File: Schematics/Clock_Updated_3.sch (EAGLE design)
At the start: 48 parts, among them U1 ATMEGA328P

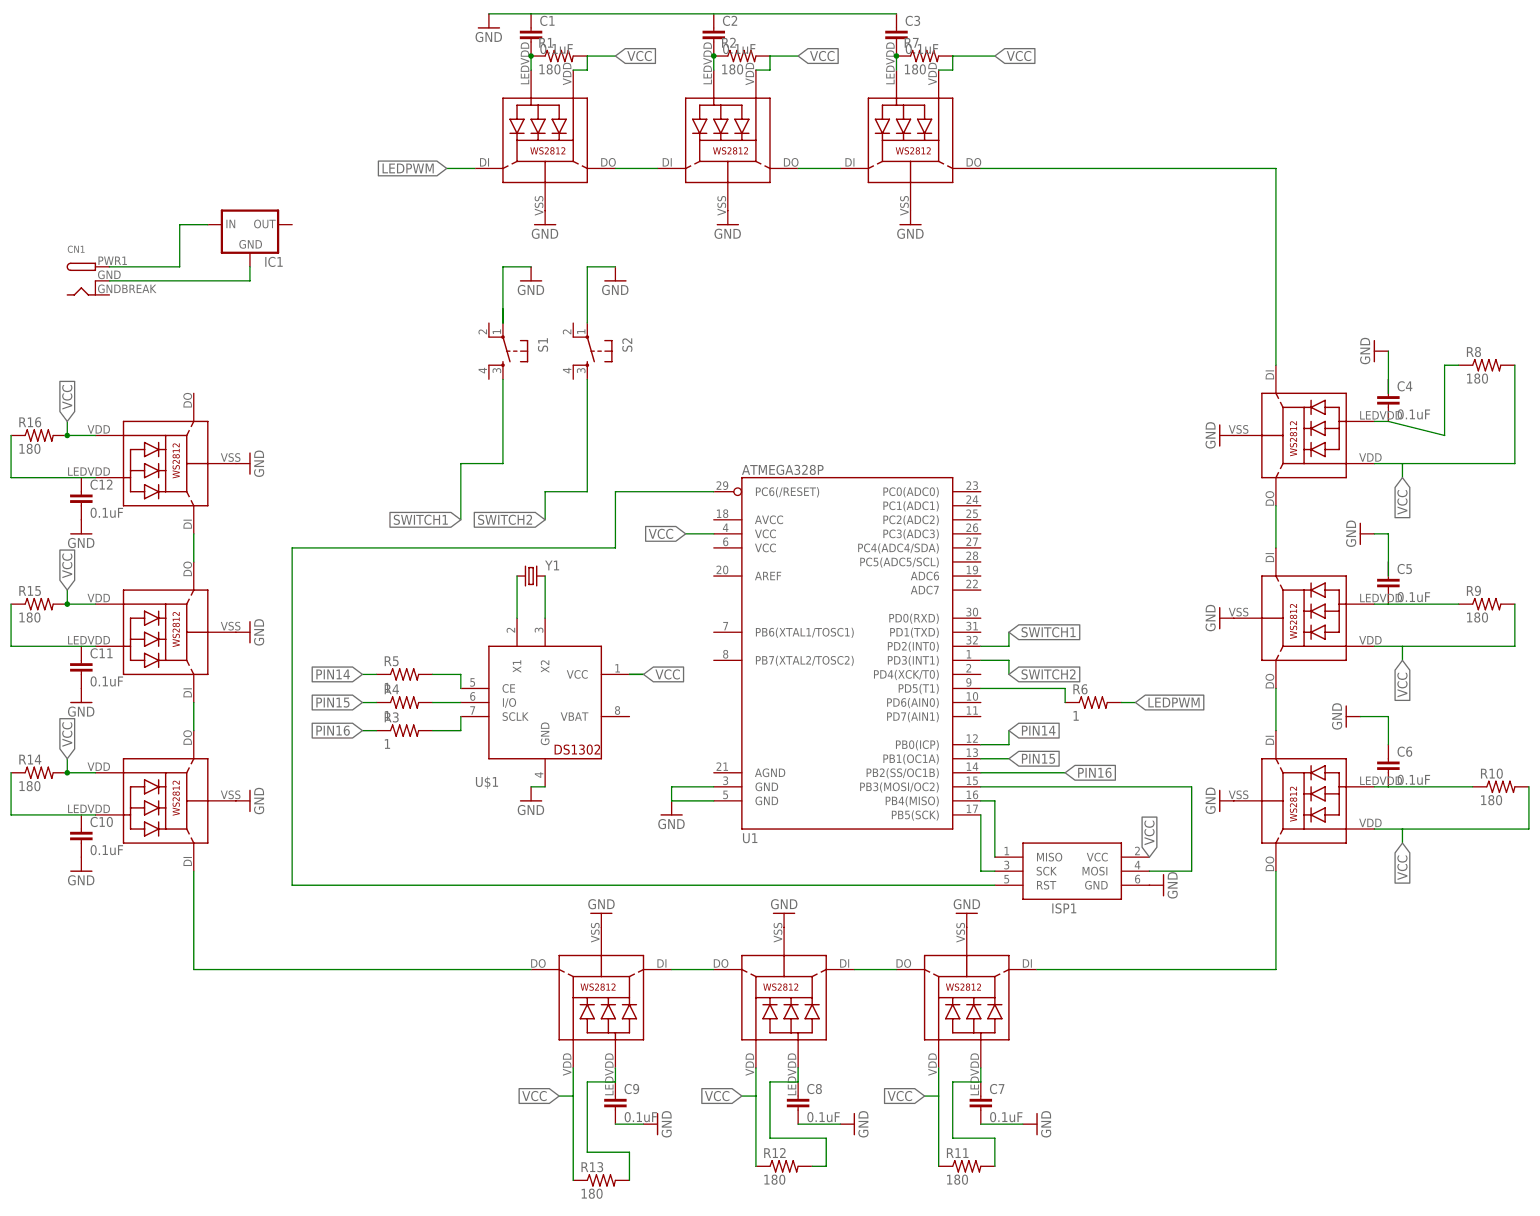
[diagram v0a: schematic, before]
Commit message: line color change
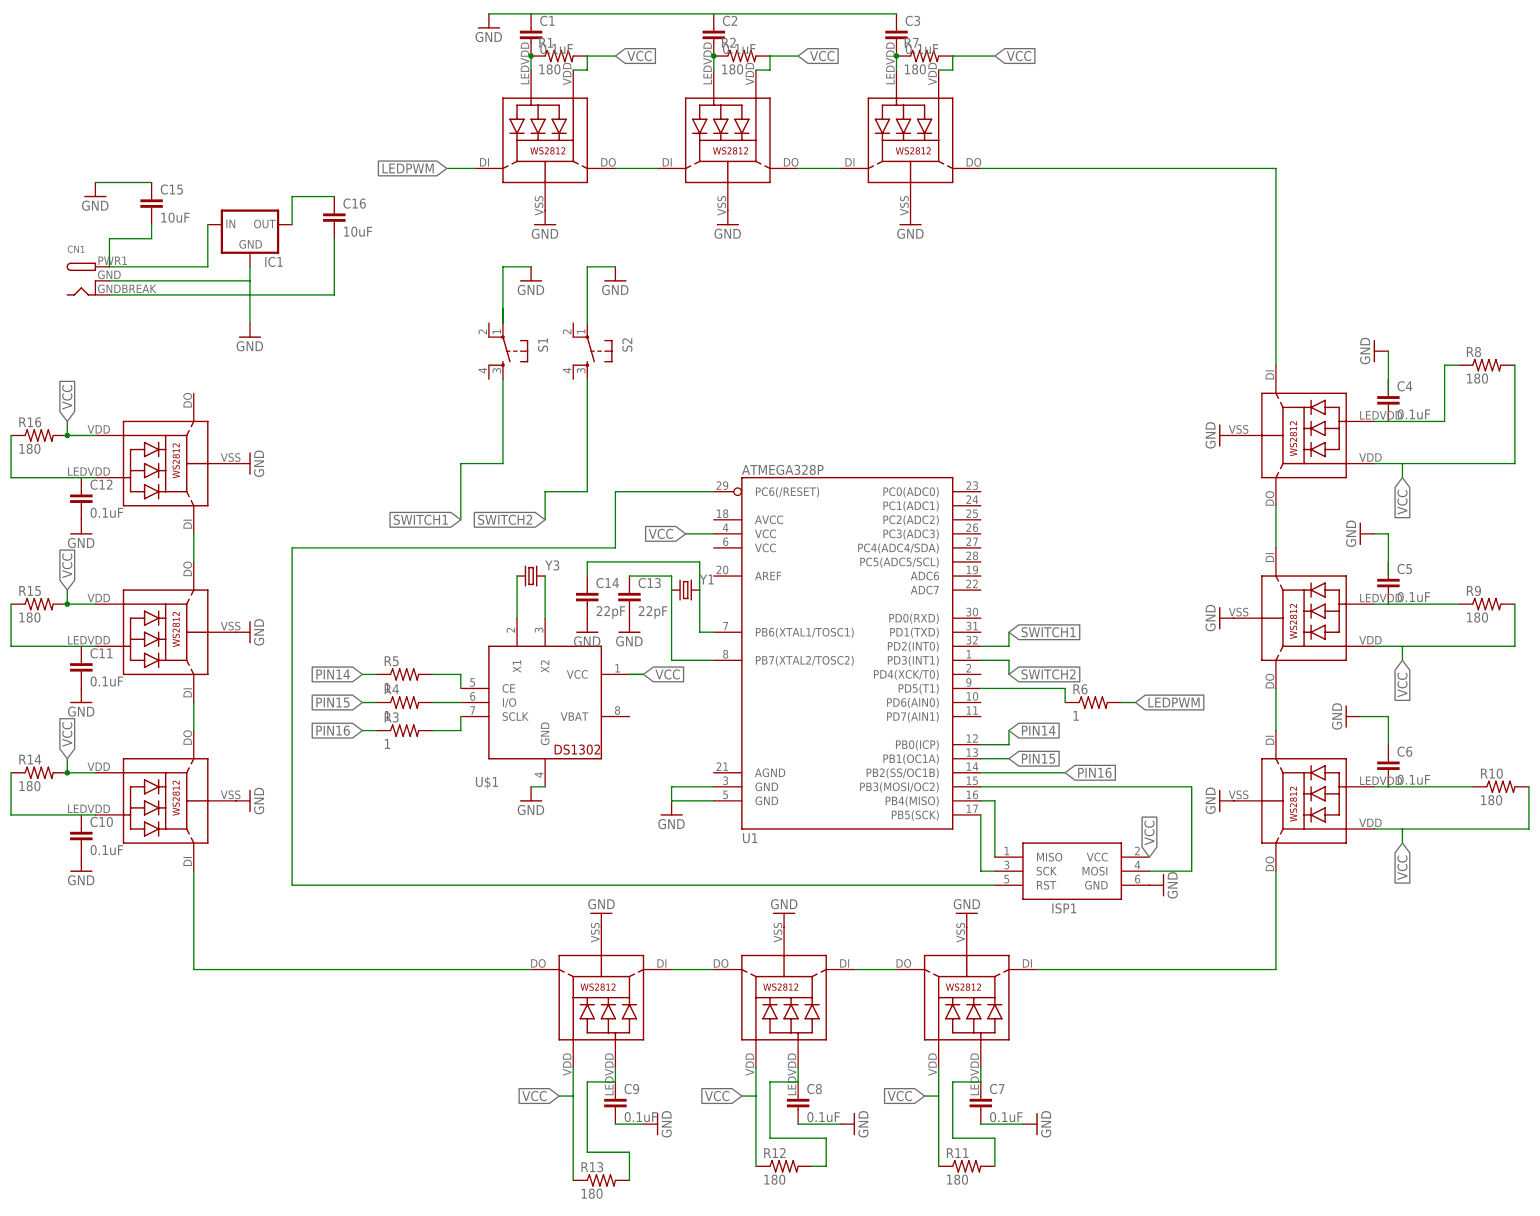
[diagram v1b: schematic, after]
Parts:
- added C13, C14: 22pF, SparkFun-Capacitors:22PF-50V-5%(0603)
- added C15, C16: 10uF, SparkFun-Capacitors:10UF-6.3V-20%(1206)
- added Y3: (no value), SparkFun-FreqCtrl:CRYSTAL32-SMD
- Y1: device SparkFun-FreqCtrl:CRYSTALTC38H -> SparkFun-FreqCtrl:CRYSTALSMD
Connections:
- new net N$38: C13.1, U1.PB7(XTAL2/TOSC2), Y1.1
- new net N$39: C14.1, U1.PB6(XTAL1/TOSC1), Y1.2
- net GND: now also C13.2, C14.2, C15.1, C16.2, CN1.GND, CN1.GNDBREAK, IC1.GND
- net N$36: now also C15.2
- net N$37: now also C16.1, IC1.OUT; no longer CN1.GNDBREAK, IC1.GND
- net N$7: now also Y3.2; no longer Y1.2
- net N$8: now also Y3.1; no longer Y1.1
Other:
- moved on the sheet: Y1
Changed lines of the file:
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@@
 </classes>
 <parts>
-<part name="Y1" library="SparkFun-FreqCtrl" deviceset="CRYSTAL" device="TC38H"/>
 <part name="S1" library="SparkFun-Electromechanical" deviceset="TAC_SWITCH" device="PTH"/>
 <part name="S2" library="SparkFun-Electromechanical" deviceset="TAC_SWITCH" device="PTH"/>
@@
 <part name="GND26" library="supply1" deviceset="GND" device=""/>
 <part name="GND27" library="supply1" deviceset="GND" device=""/>
+<part name="C13" library="SparkFun-Capacitors" deviceset="22PF-50V-5%(0603)" device="" value="22pF"/>
+<part name="C14" library="SparkFun-Capacitors" deviceset="22PF-50V-5%(0603)" device="" value="22pF"/>
+<part name="GND28" library="supply1" deviceset="GND" device=""/>
+<part name="GND29" library="supply1" deviceset="GND" device=""/>
+<part name="Y3" library="SparkFun-FreqCtrl" deviceset="CRYSTAL" device="32-SMD"/>
+<part name="Y1" library="SparkFun-FreqCtrl" deviceset="CRYSTAL" device="SMD"/>
+<part name="GND30" library="supply1" deviceset="GND" device=""/>
+<part name="C15" library="SparkFun-Capacitors" deviceset="10UF-6.3V-20%(1206)" device="" value="10uF"/>
+<part name="C16" library="SparkFun-Capacitors" deviceset="10UF-6.3V-20%(1206)" device="" value="10uF"/>
+<part name="GND31" library="supply1" deviceset="GND" device=""/>
 </parts>
 <sheets>
@@
 </plain>
 <instances>
-<instance part="Y1" gate="G$1" x="30.48" y="53.34"/>
 <instance part="S1" gate="S" x="25.4" y="93.98" rot="R270"/>
 <instance part="S2" gate="S" x="40.64" y="93.98" rot="R270"/>
@@
 <instance part="GND26" gate="1" x="-50.8" y="0"/>
 <instance part="GND27" gate="1" x="144.78" y="-2.54" rot="R90"/>
+<instance part="C13" gate="G$1" x="48.26" y="48.26"/>
+<instance part="C14" gate="G$1" x="40.64" y="48.26"/>
+<instance part="GND28" gate="1" x="48.26" y="43.18"/>
+<instance part="GND29" gate="1" x="40.64" y="43.18"/>
+<instance part="Y3" gate="G$1" x="30.48" y="53.34"/>
+<instance part="Y1" gate="G$1" x="58.42" y="50.8"/>
+<instance part="GND30" gate="1" x="-20.32" y="96.52"/>
+<instance part="C15" gate="G$1" x="-38.1" y="119.38"/>
+<instance part="C16" gate="G$1" x="-5.08" y="116.84"/>
+<instance part="GND31" gate="1" x="-48.26" y="121.92"/>
 </instances>
 <busses>
@@
 <segment>
 <pinref part="U$1" gate="G$1" pin="X2"/>
-<pinref part="Y1" gate="G$1" pin="2"/>
 <wire x1="33.02" y1="53.34" x2="33.02" y2="45.72" width="0.1524" layer="91"/>
+<pinref part="Y3" gate="G$1" pin="2"/>
 </segment>
 </net>
@@
 <segment>
 <pinref part="U$1" gate="G$1" pin="X1"/>
-<pinref part="Y1" gate="G$1" pin="1"/>
 <wire x1="27.94" y1="53.34" x2="27.94" y2="45.72" width="0.1524" layer="91"/>
+<pinref part="Y3" gate="G$1" pin="1"/>
 </segment>
 </net>
@@
 <pinref part="ISP1" gate="G$1" pin="GND"/>
 <pinref part="GND27" gate="1" pin="GND"/>
+</segment>
+<segment>
+<pinref part="C13" gate="G$1" pin="2"/>
+<pinref part="GND28" gate="1" pin="GND"/>
+</segment>
+<segment>
+<pinref part="C14" gate="G$1" pin="2"/>
+<pinref part="GND29" gate="1" pin="GND"/>
+</segment>
+<segment>
+<pinref part="CN1" gate="G$1" pin="GNDBREAK"/>
+<pinref part="IC1" gate="G$1" pin="GND"/>
+<wire x1="-45.72" y1="106.68" x2="-20.32" y2="106.68" width="0.1524" layer="91"/>
+<wire x1="-20.32" y1="106.68" x2="-20.32" y2="109.22" width="0.1524" layer="91"/>
+<pinref part="CN1" gate="G$1" pin="GND"/>
+<wire x1="-45.72" y1="104.14" x2="-20.32" y2="104.14" width="0.1524" layer="91"/>
+<wire x1="-20.32" y1="104.14" x2="-20.32" y2="106.68" width="0.1524" layer="91"/>
+<wire x1="-20.32" y1="104.14" x2="-20.32" y2="99.06" width="0.1524" layer="91"/>
+<pinref part="GND30" gate="1" pin="GND"/>
+<pinref part="C16" gate="G$1" pin="2"/>
+<wire x1="-5.08" y1="114.3" x2="-5.08" y2="104.14" width="0.1524" layer="91"/>
+<wire x1="-5.08" y1="104.14" x2="-20.32" y2="104.14" width="0.1524" layer="91"/>
+</segment>
+<segment>
+<pinref part="GND31" gate="1" pin="GND"/>
+<pinref part="C15" gate="G$1" pin="1"/>
+<wire x1="-48.26" y1="124.46" x2="-38.1" y2="124.46" width="0.1524" layer="91"/>
 </segment>
 </net>
@@
 <wire x1="182.88" y1="81.28" x2="185.42" y2="81.28" width="0.1524" layer="91"/>
 <pinref part="C4" gate="G$1" pin="2"/>
+<wire x1="185.42" y1="81.28" x2="195.58" y2="81.28" width="0.1524" layer="91"/>
 <pinref part="R8" gate="G$1" pin="1"/>
 <wire x1="198.12" y1="91.44" x2="195.58" y2="91.44" width="0.1524" layer="91"/>
-<wire x1="195.58" y1="91.44" x2="195.58" y2="78.74" width="0.1524" layer="91"/>
-<wire x1="195.58" y1="78.74" x2="185.42" y2="81.28" width="0.1524" layer="91"/>
+<wire x1="195.58" y1="81.28" x2="195.58" y2="91.44" width="0.1524" layer="91"/>
 </segment>
 </net>
@@
 <segment>
 <pinref part="CN1" gate="G$1" pin="PWR"/>
-<wire x1="-45.72" y1="109.22" x2="-33.02" y2="109.22" width="0.1524" layer="91"/>
-<wire x1="-33.02" y1="109.22" x2="-33.02" y2="116.84" width="0.1524" layer="91"/>
+<wire x1="-45.72" y1="109.22" x2="-27.94" y2="109.22" width="0.1524" layer="91"/>
+<wire x1="-45.72" y1="109.22" x2="-45.72" y2="114.3" width="0.1524" layer="91"/>
+<pinref part="C15" gate="G$1" pin="2"/>
+<wire x1="-45.72" y1="114.3" x2="-38.1" y2="114.3" width="0.1524" layer="91"/>
+<wire x1="-38.1" y1="114.3" x2="-38.1" y2="116.84" width="0.1524" layer="91"/>
 <pinref part="IC1" gate="G$1" pin="IN"/>
-<wire x1="-33.02" y1="116.84" x2="-27.94" y2="116.84" width="0.1524" layer="91"/>
+<wire x1="-27.94" y1="109.22" x2="-27.94" y2="116.84" width="0.1524" layer="91"/>
+</segment>
+</net>
+<net name="N$38" class="0">
+<segment>
+<wire x1="55.88" y1="53.34" x2="55.88" y2="50.8" width="0.1524" layer="91"/>
+<pinref part="U1" gate="G$1" pin="PB7(XTAL2/TOSC2)"/>
+<wire x1="55.88" y1="50.8" x2="55.88" y2="38.1" width="0.1524" layer="91"/>
+<wire x1="55.88" y1="38.1" x2="63.5" y2="38.1" width="0.1524" layer="91"/>
+<pinref part="C13" gate="G$1" pin="1"/>
+<wire x1="55.88" y1="53.34" x2="48.26" y2="53.34" width="0.1524" layer="91"/>
+<pinref part="Y1" gate="G$1" pin="1"/>
+</segment>
+</net>
+<net name="N$39" class="0">
+<segment>
+<pinref part="U1" gate="G$1" pin="PB6(XTAL1/TOSC1)"/>
+<wire x1="63.5" y1="43.18" x2="60.96" y2="43.18" width="0.1524" layer="91"/>
+<pinref part="C14" gate="G$1" pin="1"/>
+<wire x1="40.64" y1="53.34" x2="40.64" y2="55.88" width="0.1524" layer="91"/>
+<wire x1="40.64" y1="55.88" x2="60.96" y2="55.88" width="0.1524" layer="91"/>
+<wire x1="60.96" y1="55.88" x2="60.96" y2="50.8" width="0.1524" layer="91"/>
+<pinref part="Y1" gate="G$1" pin="2"/>
+<wire x1="60.96" y1="50.8" x2="60.96" y2="43.18" width="0.1524" layer="91"/>
 </segment>
 </net>
 <net name="N$37" class="0">
 <segment>
-<pinref part="CN1" gate="G$1" pin="GNDBREAK"/>
-<pinref part="IC1" gate="G$1" pin="GND"/>
-<wire x1="-45.72" y1="106.68" x2="-20.32" y2="106.68" width="0.1524" layer="91"/>
-<wire x1="-20.32" y1="106.68" x2="-20.32" y2="109.22" width="0.1524" layer="91"/>
-</segment>
-</net>
+<pinref part="IC1" gate="G$1" pin="OUT"/>
+<wire x1="-12.7" y1="116.84" x2="-12.7" y2="121.92" width="0.1524" layer="91"/>
+<pinref part="C16" gate="G$1" pin="1"/>
+<wire x1="-5.08" y1="121.92" x2="-12.7" y2="121.92" width="0.1524" layer="91"/>
+</segment>
+</net>
